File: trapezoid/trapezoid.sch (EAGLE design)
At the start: 29 parts, among them IC2 LGD20H, U1 MMA8452Q, U2 microSD, U3 DS3234, U4 MCP73831

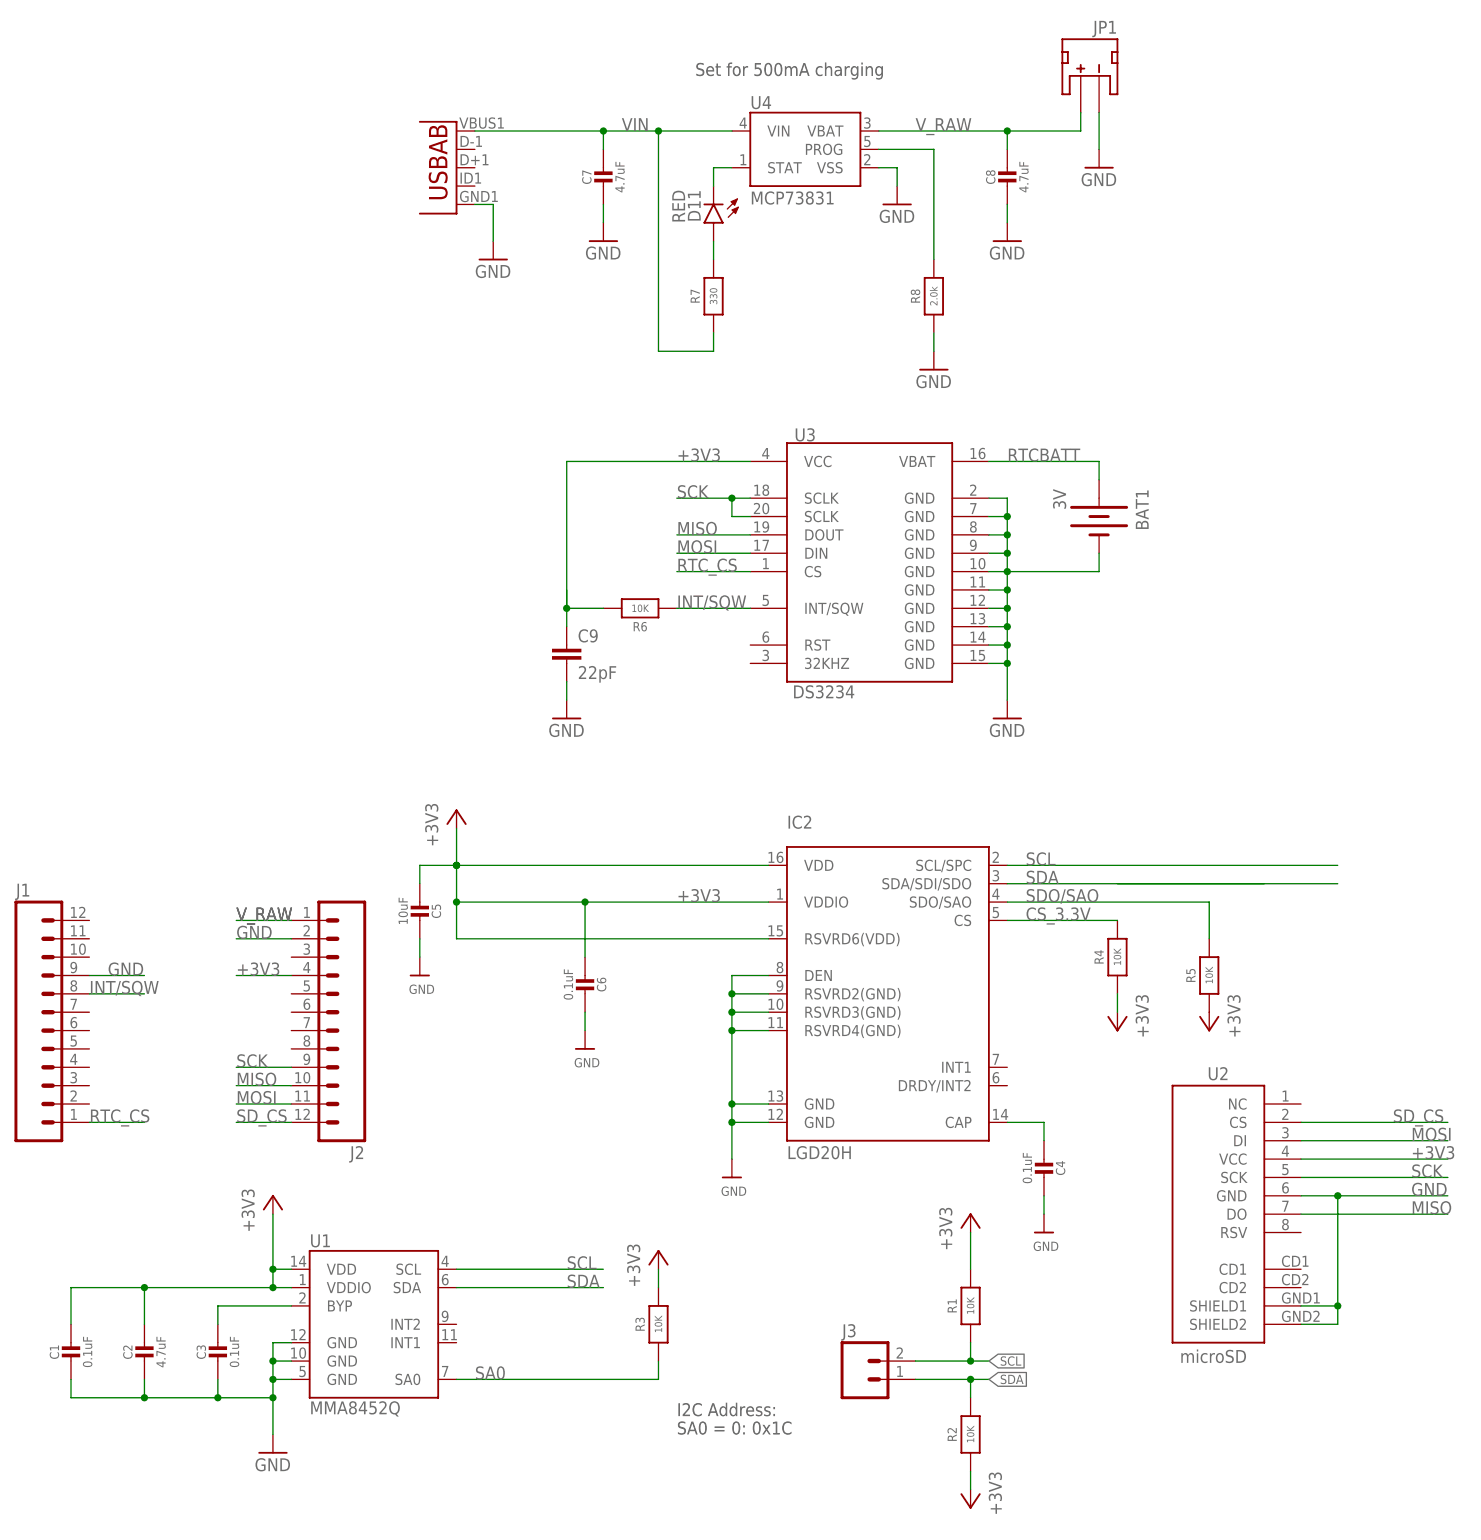
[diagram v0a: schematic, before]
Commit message: chnaged rtc to ds1339b in trap
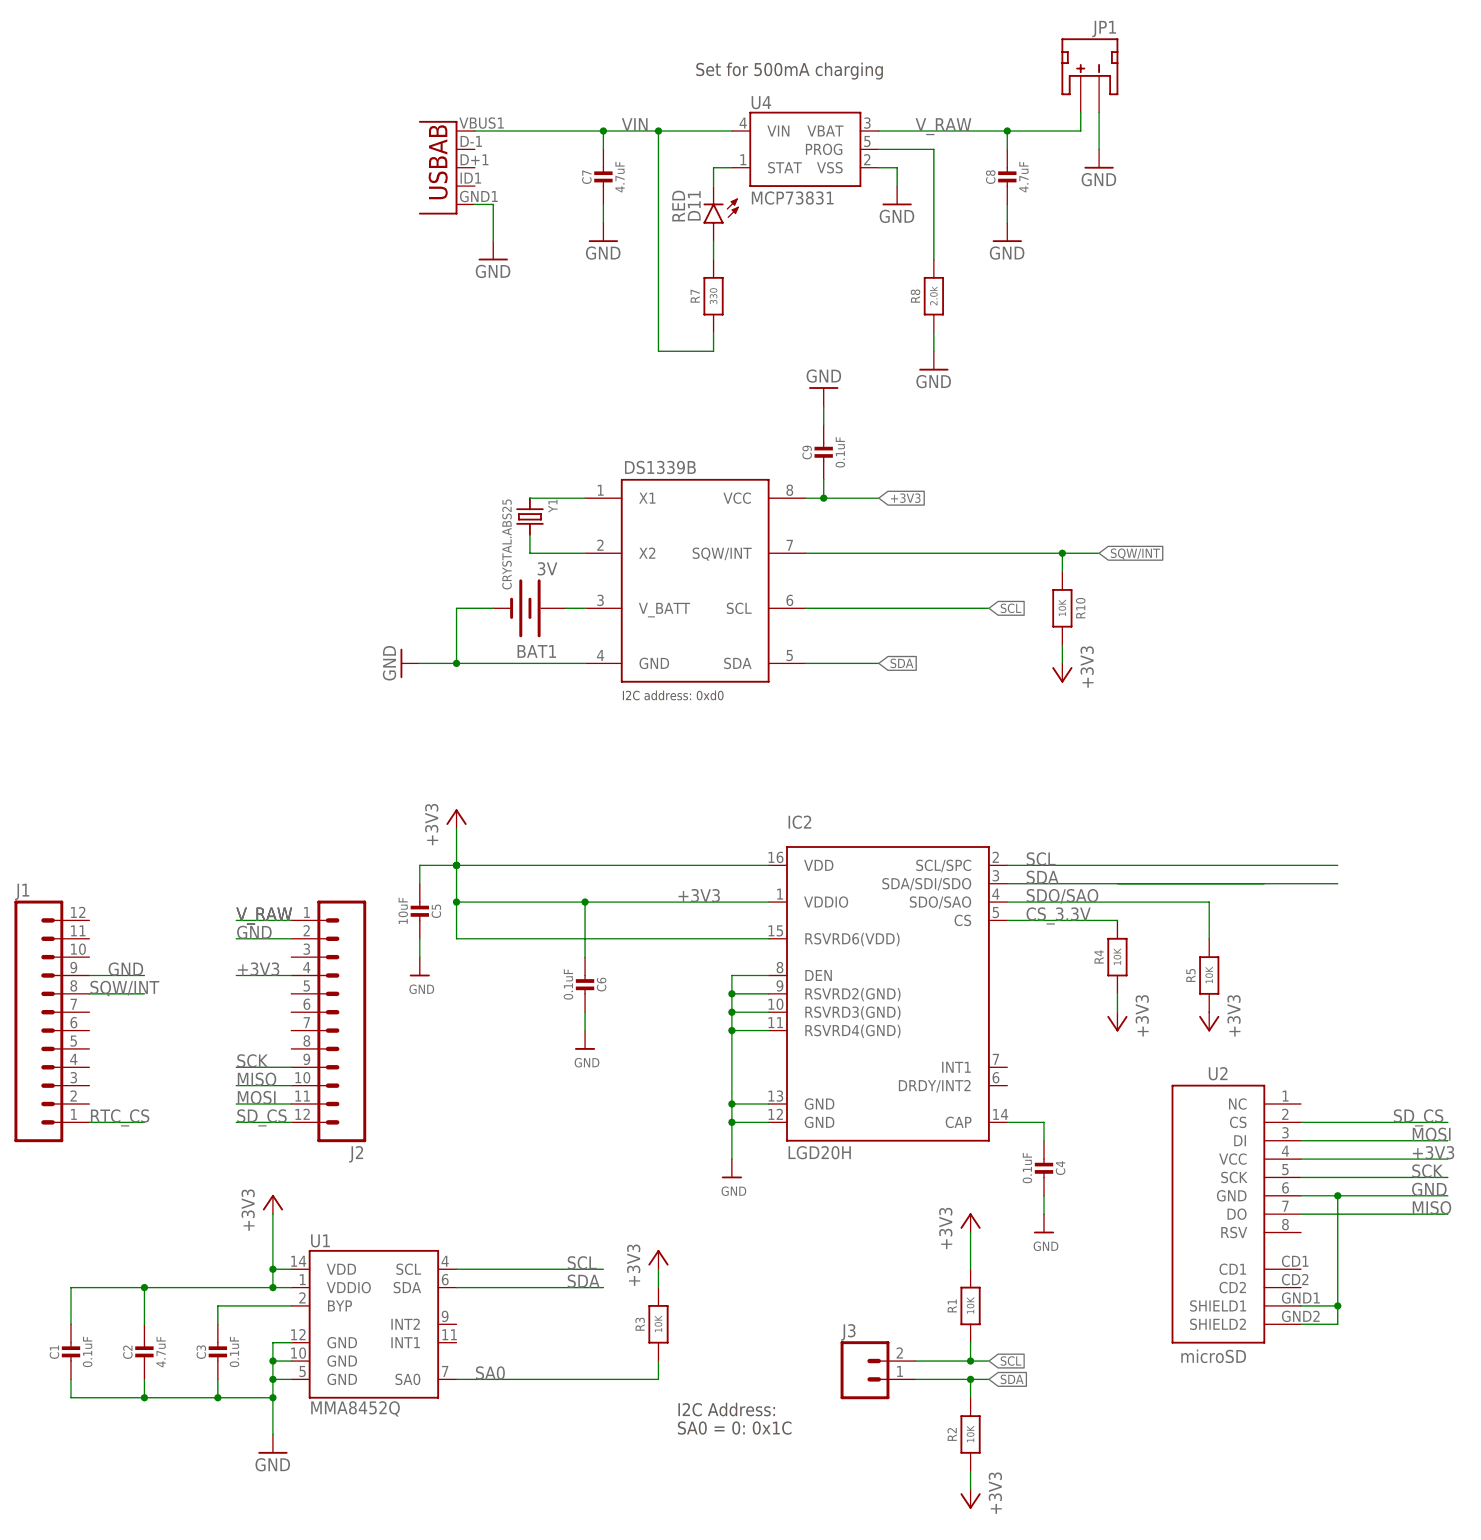
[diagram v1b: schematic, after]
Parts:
- removed R6: 10K, microbuilder:RESISTOR_0805MP
- removed U3: DS3234, SparkFun:DS3234
- added R10: 10K, microbuilder:RESISTOR0805_NOOUTLINE
- added U$3: DS1339BDS1339B, sharkdunio:DS1339BDS1339B
- added Y1: CRYSTAL.ABS25, abracon:CRYSTAL.ABS25
- C9: value 22pF -> 0.1uF; device SparkFun:CAP0402-CAP -> microbuilder:CAP_CERAMIC0805-NOOUTLINE
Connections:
- removed net INT/SQW: J1.8, U3.INT/SQW
- removed net RTCBATT: BAT1.+, U3.VBAT
- new net N$2: U$3.X2, Y1.2
- new net N$4: BAT1.+, U$3.V_BATT
- new net N$5: U$3.X1, Y1.1
- new net SQW/INT: J1.8, R10.1, U$3.SQW/INT
- net +3V3: now also C9.2, R10.2, U$3.VCC; no longer C9.1, R6.2, U3.VCC
- net GND: now also C9.1, U$3.GND; no longer C9.2, U3.GND, U3.GND@10, U3.GND@11, U3.GND@12, U3.GND@13, U3.GND@14, U3.GND@2, U3.GND@7, U3.GND@8, U3.GND@9
- net MISO: no longer U3.DOUT
- net MOSI: no longer U3.DIN
- net RTC_CS: no longer U3.CS
- net SCK: no longer U3.SCLK@18, U3.SCLK@20
- net SCL: now also U$3.SCL
- net SDA: now also U$3.SDA
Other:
- note added: "I2C address: 0xd0"
- moved on the sheet: BAT1, C9

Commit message: placed rtc and usd
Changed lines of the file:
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@@
-</segment>
-<segment>
-<wire x1="139.7" y1="91.44" x2="185.42" y2="91.44" width="0.1524" layer="91"/>
-<label x="142.24" y="91.44" size="1.778" layer="95"/>
-<pinref part="IC2" gate="G$1" pin="SDA/SDI/SDO"/>
 </segment>
 <segment>
@@
 <wire x1="111.76" y1="121.92" x2="121.92" y2="121.92" width="0.1524" layer="91"/>
 <label x="121.92" y="121.92" size="1.27" layer="95" xref="yes"/>
+</segment>
+<segment>
+<pinref part="IC2" gate="G$1" pin="SDA/SDI/SDO"/>
+<wire x1="139.7" y1="91.44" x2="162.56" y2="91.44" width="0.1524" layer="91"/>
+<label x="162.56" y="91.44" size="1.27" layer="95" xref="yes"/>
 </segment>
 </net>
@@
 </segment>
 </net>
-<net name="N$8" class="0">
-<segment>
-<wire x1="154.94" y1="91.44" x2="175.26" y2="91.44" width="0.1524" layer="91"/>
-</segment>
-</net>

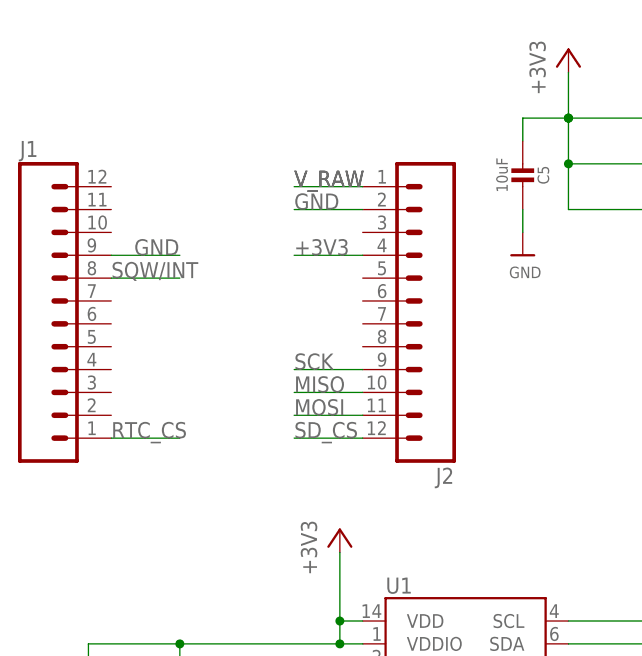
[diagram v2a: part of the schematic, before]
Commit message: fully connected schematics
had to remove some header pin spots to run wire
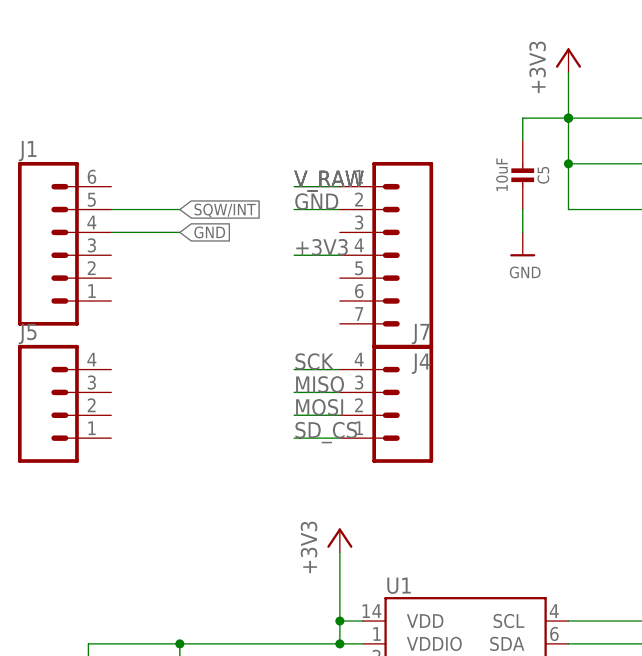
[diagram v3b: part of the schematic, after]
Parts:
- removed J2: (no value), SparkFun-Connectors:M12PTH
- added J4: (no value), SparkFun-Connectors:M07
- added J5, J7: (no value), SparkFun-Connectors:M04PTH
- J1: device SparkFun-Connectors:M12PTH -> SparkFun-Connectors:M06SILK_FEMALE_PTH
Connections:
- removed net RTC_CS: J1.1
- net +3V3: now also J4.4; no longer J2.4
- net GND: now also J1.4, J4.2; no longer J1.9, J2.2
- net MISO: now also J7.3; no longer J2.10
- net MOSI: now also J7.2; no longer J2.11
- net SCK: now also J7.4; no longer J2.9
- net SD_CS: now also J7.1; no longer J2.12
- net SQW/INT: now also J1.5; no longer J1.8
- net V_RAW: now also J4.1; no longer J2.1
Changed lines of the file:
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@@
 <layers>
 <layer number="1" name="Top" color="4" fill="1" visible="no" active="no"/>
+<layer number="2" name="Route2" color="1" fill="3" visible="no" active="no"/>
+<layer number="3" name="Route3" color="4" fill="3" visible="no" active="no"/>
+<layer number="14" name="Route14" color="1" fill="6" visible="no" active="no"/>
+<layer number="15" name="Route15" color="4" fill="6" visible="no" active="no"/>
 <layer number="16" name="Bottom" color="1" fill="1" visible="no" active="no"/>
 <layer number="17" name="Pads" color="2" fill="1" visible="no" active="no"/>
@@
 <part name="GND1" library="SparkFun" deviceset="GND" device=""/>
 <part name="U2" library="SparkFun" deviceset="USD-SOCKET" device="SMD" value="microSD"/>
-<part name="J1" library="SparkFun-Connectors" deviceset="M12" device="PTH"/>
-<part name="J2" library="SparkFun-Connectors" deviceset="M12" device="PTH"/>
 <part name="J3" library="SparkFun-Connectors" deviceset="M02" device="LOCK"/>
 <part name="C4" library="microbuilder" deviceset="CAP_CERAMIC" device="0805-NOOUTLINE" value="0.1uF"/>
@@
 <part name="GND2" library="SparkFun" deviceset="GND" device=""/>
 <part name="GND3" library="SparkFun" deviceset="GND" device=""/>
+<part name="J5" library="SparkFun-Connectors" deviceset="M04" device="PTH"/>
+<part name="J1" library="SparkFun-Connectors" deviceset="M06" device="SILK_FEMALE_PTH"/>
+<part name="J7" library="SparkFun-Connectors" deviceset="M04" device="PTH"/>
+<part name="J4" library="SparkFun-Connectors" deviceset="M07" device=""/>
 </parts>
 <sheets>
@@
 <attribute name="VALUE" x="163.576" y="25.146" size="1.778" layer="96"/>
 </instance>
-<instance part="J1" gate="G$1" x="2.54" y="73.66"/>
-<instance part="J2" gate="G$1" x="50.8" y="71.12" rot="R180"/>
 <instance part="J3" gate="G$1" x="119.38" y="22.86"/>
 <instance part="C4" gate="G$1" x="144.78" y="53.34" rot="R180"/>
@@
 <instance part="GND2" gate="1" x="114.3" y="160.02" rot="R180"/>
 <instance part="GND3" gate="1" x="55.88" y="121.92" rot="R270"/>
+<instance part="J5" gate="G$1" x="7.62" y="60.96"/>
+<instance part="J1" gate="G$1" x="7.62" y="78.74"/>
+<instance part="J7" gate="G$1" x="43.18" y="60.96" rot="MR0"/>
+<instance part="J4" gate="G$1" x="43.18" y="81.28" rot="R180"/>
 </instances>
 <busses>
@@
 </segment>
 <segment>
-<wire x1="12.7" y1="78.74" x2="20.32" y2="78.74" width="0.1524" layer="91"/>
-<label x="15.24" y="78.74" size="1.778" layer="95"/>
-<pinref part="J1" gate="G$1" pin="9"/>
-</segment>
-<segment>
-<wire x1="40.64" y1="83.82" x2="33.02" y2="83.82" width="0.1524" layer="91"/>
 <label x="33.02" y="83.82" size="1.778" layer="95"/>
-<pinref part="J2" gate="G$1" pin="2"/>
+<pinref part="J4" gate="G$1" pin="2"/>
+<wire x1="38.1" y1="83.82" x2="33.02" y2="83.82" width="0.1524" layer="91"/>
 </segment>
 <segment>
@@
 <pinref part="GND3" gate="1" pin="GND"/>
 </segment>
+<segment>
+<wire x1="12.7" y1="81.28" x2="20.32" y2="81.28" width="0.1524" layer="91"/>
+<label x="20.32" y="81.28" size="1.27" layer="95" xref="yes"/>
+<pinref part="J1" gate="G$1" pin="4"/>
+</segment>
 </net>
 <net name="SCL" class="0">
@@
 </segment>
 <segment>
-<wire x1="40.64" y1="58.42" x2="33.02" y2="58.42" width="0.1524" layer="91"/>
 <label x="33.02" y="58.42" size="1.778" layer="95"/>
-<pinref part="J2" gate="G$1" pin="12"/>
+<pinref part="J7" gate="G$1" pin="1"/>
+<wire x1="38.1" y1="58.42" x2="33.02" y2="58.42" width="0.1524" layer="91"/>
 </segment>
 </net>
@@
 </segment>
 <segment>
-<wire x1="40.64" y1="60.96" x2="33.02" y2="60.96" width="0.1524" layer="91"/>
 <label x="33.02" y="60.96" size="1.778" layer="95"/>
-<pinref part="J2" gate="G$1" pin="11"/>
+<pinref part="J7" gate="G$1" pin="2"/>
+<wire x1="38.1" y1="60.96" x2="33.02" y2="60.96" width="0.1524" layer="91"/>
 </segment>
 </net>
@@
 </segment>
 <segment>
-<wire x1="40.64" y1="66.04" x2="33.02" y2="66.04" width="0.1524" layer="91"/>
 <label x="33.02" y="66.04" size="1.778" layer="95"/>
-<pinref part="J2" gate="G$1" pin="9"/>
+<pinref part="J7" gate="G$1" pin="4"/>
+<wire x1="38.1" y1="66.04" x2="33.02" y2="66.04" width="0.1524" layer="91"/>
 </segment>
 </net>
@@
 </segment>
 <segment>
-<wire x1="40.64" y1="63.5" x2="33.02" y2="63.5" width="0.1524" layer="91"/>
 <label x="33.02" y="63.5" size="1.778" layer="95"/>
-<pinref part="J2" gate="G$1" pin="10"/>
-</segment>
-</net>
-<net name="RTC_CS" class="0">
-<segment>
-<wire x1="12.7" y1="58.42" x2="20.32" y2="58.42" width="0.1524" layer="91"/>
-<label x="12.7" y="58.42" size="1.778" layer="95"/>
-<pinref part="J1" gate="G$1" pin="1"/>
+<pinref part="J7" gate="G$1" pin="3"/>
+<wire x1="38.1" y1="63.5" x2="33.02" y2="63.5" width="0.1524" layer="91"/>
 </segment>
 </net>
 <net name="V_RAW" class="0">
 <segment>
-<pinref part="J2" gate="G$1" pin="1"/>
-<wire x1="40.64" y1="86.36" x2="33.02" y2="86.36" width="0.1524" layer="91"/>
 <label x="33.02" y="86.36" size="1.778" layer="95"/>
 <label x="33.02" y="86.36" size="1.778" layer="95"/>
+<pinref part="J4" gate="G$1" pin="1"/>
+<wire x1="38.1" y1="86.36" x2="33.02" y2="86.36" width="0.1524" layer="91"/>
 </segment>
 <segment>
@@
 </segment>
 <segment>
-<wire x1="40.64" y1="78.74" x2="33.02" y2="78.74" width="0.1524" layer="91"/>
 <label x="33.02" y="78.74" size="1.778" layer="95"/>
-<pinref part="J2" gate="G$1" pin="4"/>
+<pinref part="J4" gate="G$1" pin="4"/>
+<wire x1="38.1" y1="78.74" x2="33.02" y2="78.74" width="0.1524" layer="91"/>
 </segment>
 <segment>
@@
 </segment>
 <segment>
-<wire x1="12.7" y1="76.2" x2="20.32" y2="76.2" width="0.1524" layer="91"/>
-<label x="12.7" y="76.2" size="1.778" layer="95"/>
-<pinref part="J1" gate="G$1" pin="8"/>
-</segment>
-</net>
+<wire x1="12.7" y1="83.82" x2="20.32" y2="83.82" width="0.1524" layer="91"/>
+<label x="20.32" y="83.82" size="1.27" layer="95" xref="yes"/>
+<pinref part="J1" gate="G$1" pin="5"/>
+</segment>
+</net>
